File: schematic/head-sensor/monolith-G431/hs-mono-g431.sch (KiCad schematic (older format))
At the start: 51 parts, among them P1 MICROSD-SDIO-CD, P2 SWD, P3 G B Vcc, P4 NRF24L01, P5 USB_A, P6 SENSOR_CONNECTOR, P7 DEBUG_TX, Q1 IRLML6402, Q2 IRLML2502, Q3 IRLML2502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

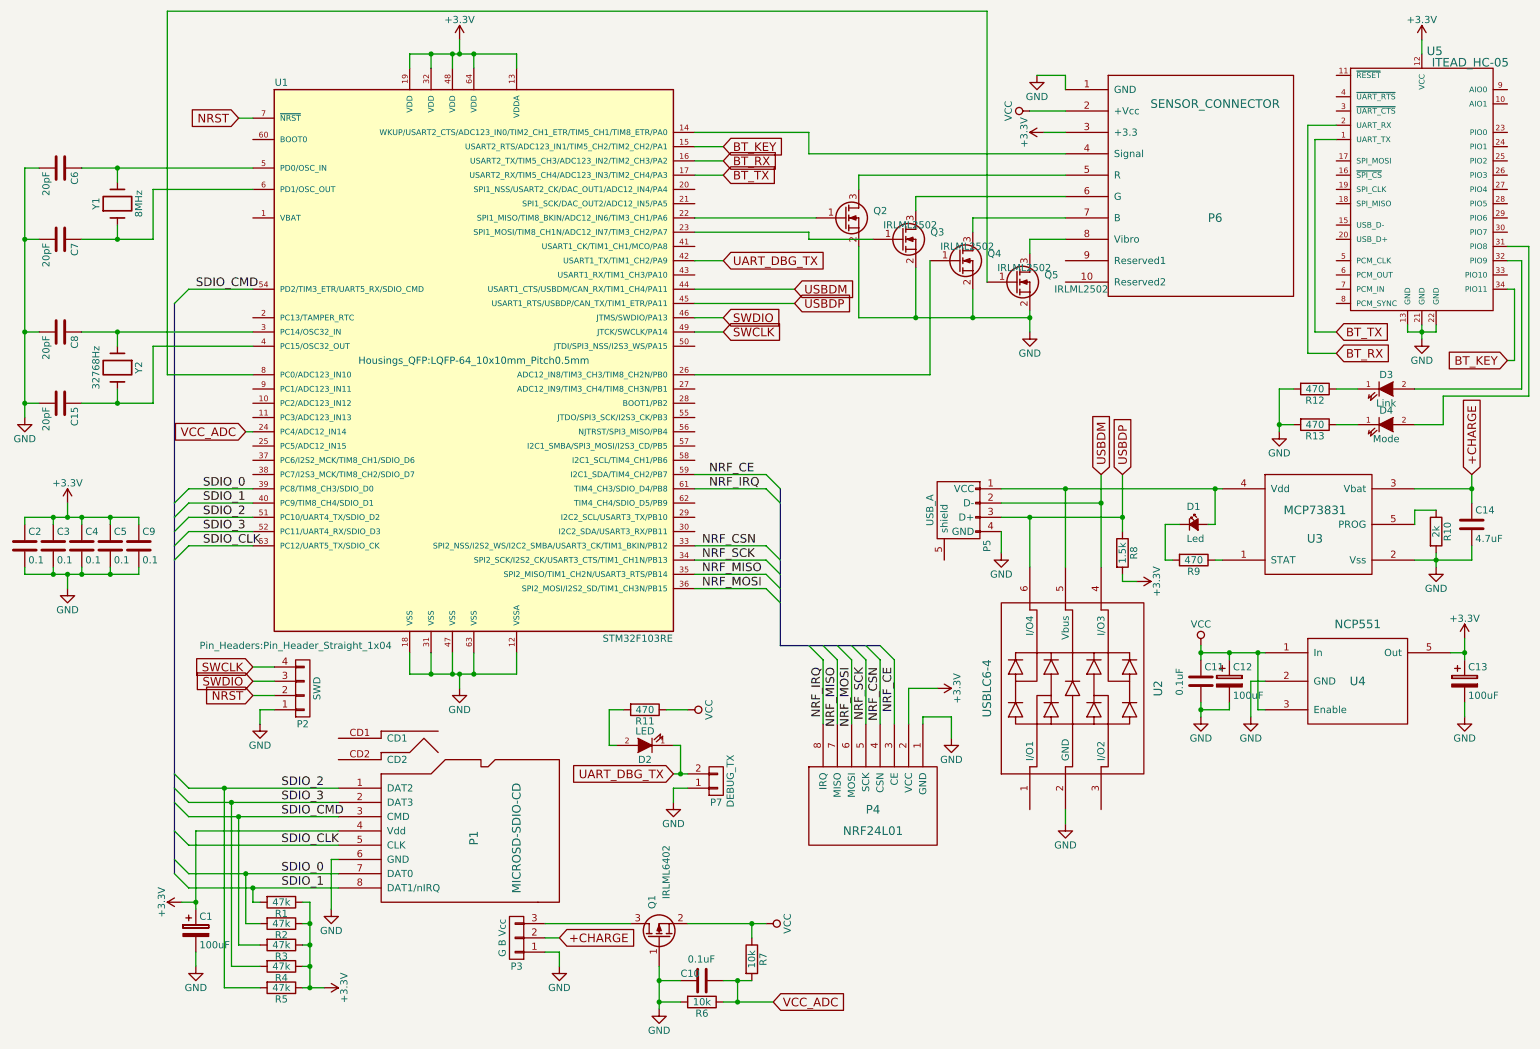
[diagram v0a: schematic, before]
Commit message: [PCB] Errors check in progress
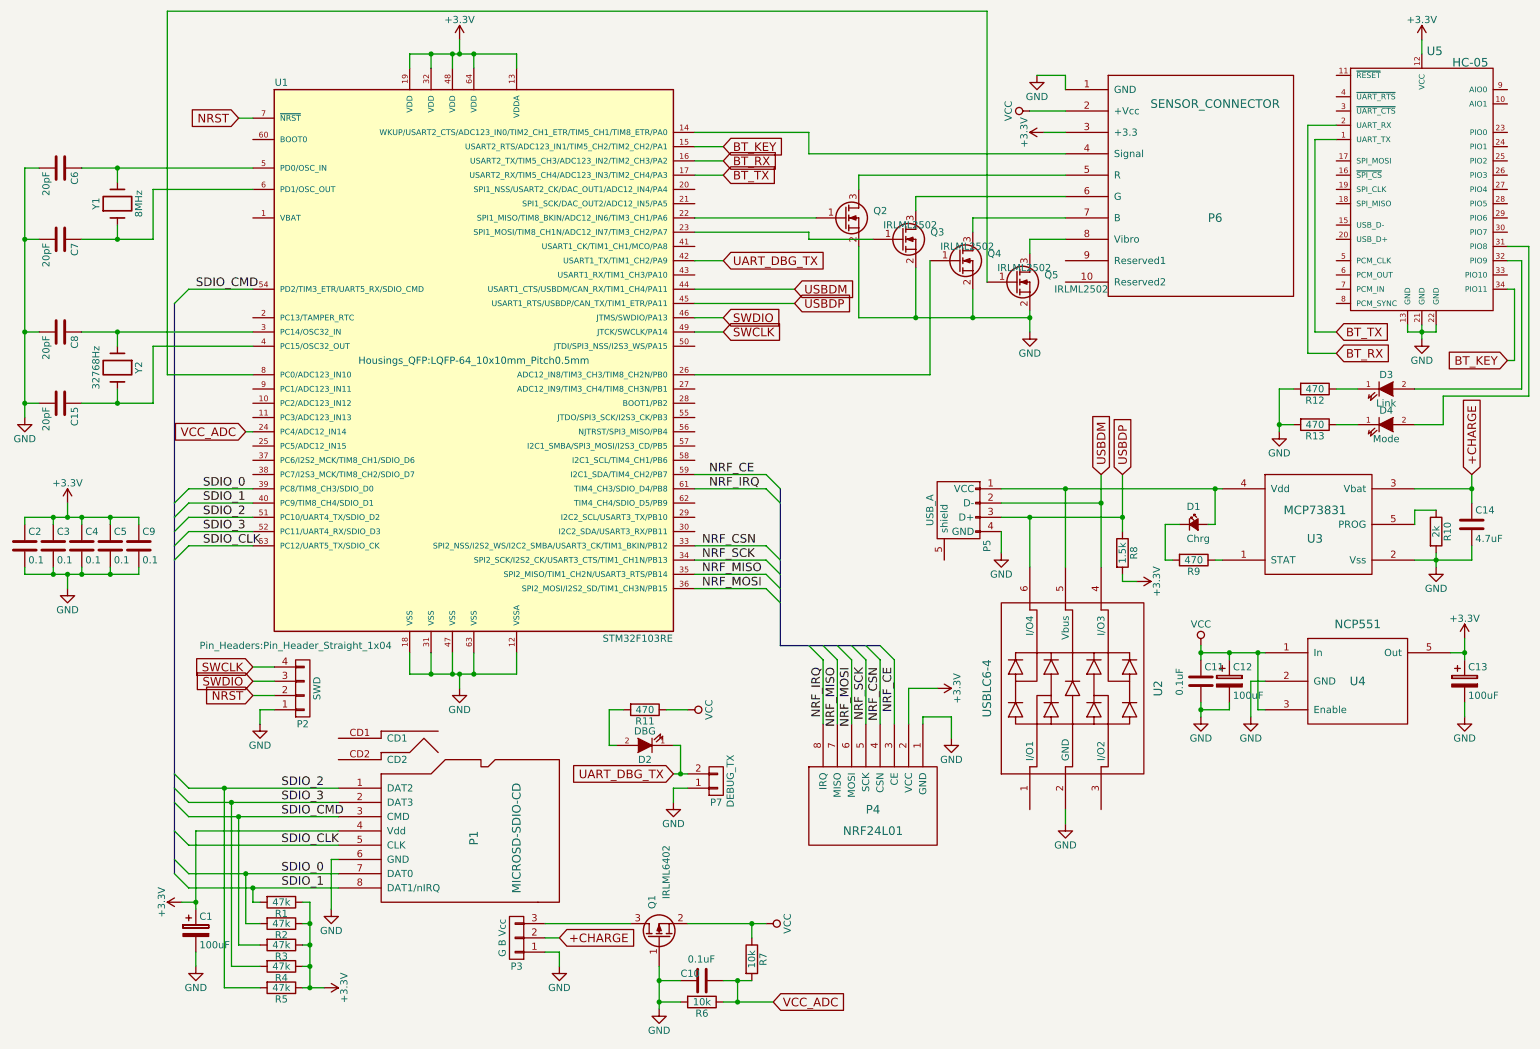
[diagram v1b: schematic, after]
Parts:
- D1: value Led -> Chrg
- D2: value LED -> DBG
- U5: value ITEAD_HC-05 -> HC-05
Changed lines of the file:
@@
 encoding utf-8
 Sheet 1 1
-Title ""
-Date ""
-Rev ""
-Comp ""
+Title "Head sensor and bluetooth bridge board"
+Date "2016-10-09"
+Rev "1.0"
+Comp "Caustic Lasertag System Project"
 Comment1 ""
-Comment2 ""
+Comment2 "Aleksey Bulatov"
 Comment3 ""
 Comment4 ""
@@
 P 8800 4200
 F 0 "D1" H 8750 4325 50  0000 L CNN
-F 1 "Led" H 8750 4100 50  0000 L CNN
+F 1 "Chrg" H 8750 4100 50  0000 L CNN
 F 2 "LEDs:LED_0805" V 8800 4200 50  0001 C CNN
 F 3 "" V 8800 4200 50  0000 C CNN
@@
 P 4950 5750
 F 0 "D2" H 4950 5850 50  0000 C CNN
-F 1 "LED" H 4950 5650 50  0000 C CNN
+F 1 "DBG" H 4950 5650 50  0000 C CNN
 F 2 "LEDs:LED_0805" H 4950 5750 50  0001 C CNN
 F 3 "" H 4950 5750 50  0000 C CNN
@@
 P 10400 1850
 F 0 "U5" H 10490 2820 60  0000 C CNN
-F 1 "ITEAD_HC-05" H 10740 2740 60  0000 C CNN
+F 1 "HC-05" H 10740 2740 60  0000 C CNN
 F 2 "w_rf_modules:ITEAD_HC-05" H 10400 1850 60  0001 C CNN
 F 3 "" H 10400 1850 60  0000 C CNN

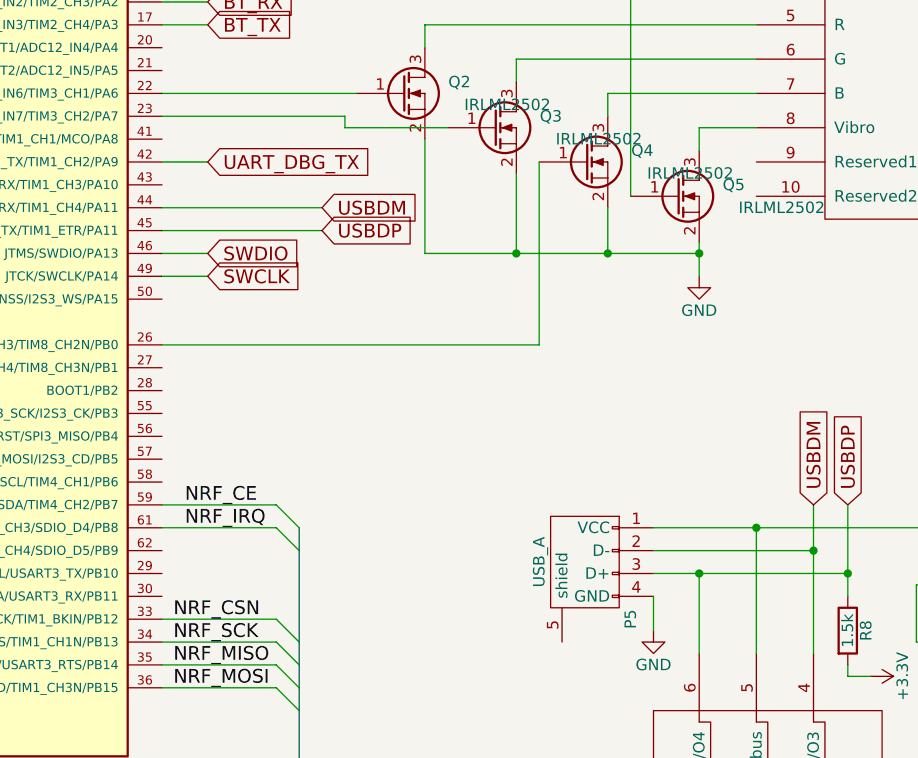
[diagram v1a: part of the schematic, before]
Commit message: [PCB] Head sensor fix: added UART/I2C pins to sensors connector
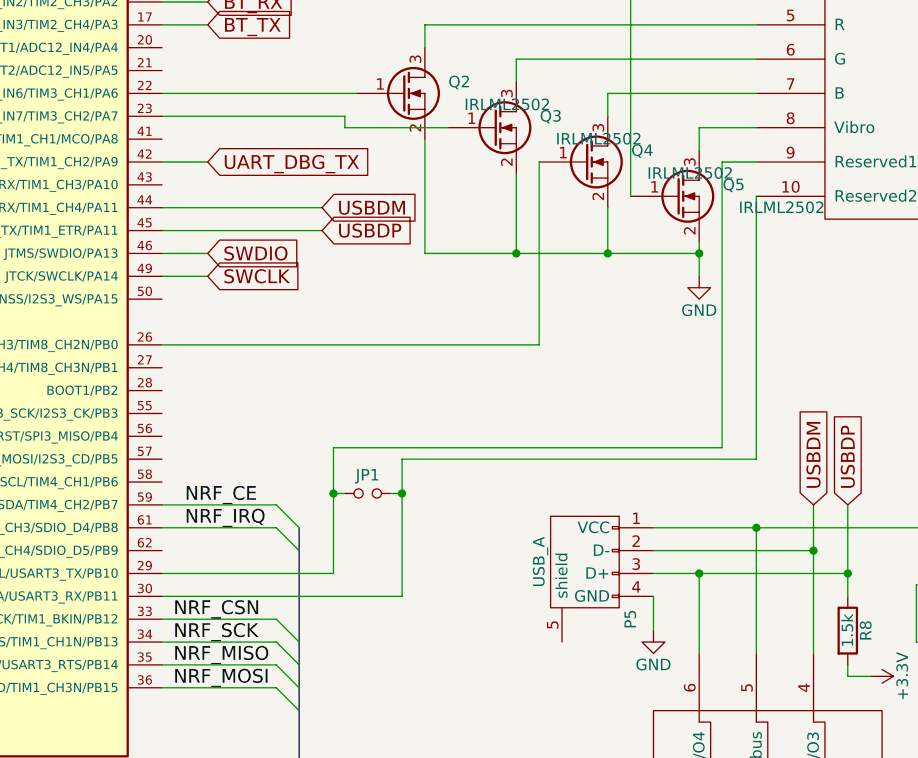
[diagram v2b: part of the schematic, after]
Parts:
- added JP1: Jumper_NO_Small, Resistors_SMD:R_0402, symbol Jumper_NO_Small
- P6: footprint Pin_Headers:Pin_Header_Straight_1x08 -> Pin_Headers:Pin_Header_Straight_1x10
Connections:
- net at U1.29 (I2C2_SCL/USART3_TX/PB10): now also P6.9 (Reserved1), JP1.1
- net at U1.30 (I2C2_SDA/USART3_RX/PB11): now also P6.10 (Reserved2), JP1.2

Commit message: PWM support for internal illumination points added, ST copyrights updated
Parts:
- D2, D3, D4: symbol LED -> LED-RESCUE-hs-mono-g431
- P5: symbol USB_A -> USB_A-RESCUE-hs-mono-g431
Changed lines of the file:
@@
 EESchema Schematic File Version 2
+LIBS:hs-mono-g431-rescue
 LIBS:power
 LIBS:device
@@
 UART_DBG_TX
 $Comp
-L USB_A P5
+L USB_A-RESCUE-hs-mono-g431 P5
 U 1 1 57F1DA65
 P 7150 4150
@@
 UART_DBG_TX
 $Comp
-L LED D2
+L LED-RESCUE-hs-mono-g431 D2
 U 1 1 57F7E967
 P 4950 5750
@@
 BT_KEY
 $Comp
-L LED D3
+L LED-RESCUE-hs-mono-g431 D3
 U 1 1 57FA8572
 P 10150 3250
@@
 $EndComp
 $Comp
-L LED D4
+L LED-RESCUE-hs-mono-g431 D4
 U 1 1 57FA908C
 P 10150 3500
